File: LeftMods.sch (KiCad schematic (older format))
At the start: 9 parts

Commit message: Change and update leftmods
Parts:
- removed LM2: MX-1.5U, MX_Alps_Hybrid:MX-1.5U-NoLED, symbol MX-1U
- LM1: value MX-1.25U -> MX-1.5U; footprint MX_Alps_Hybrid:MX-1.25U-NoLED -> MX_Alps_Hybrid:MX-1.5U-NoLED
- LM2: renamed from LM3; value MX-1.25U -> MX-1U; footprint MX_Alps_Hybrid:MX-1.25U-NoLED -> MX_Alps_Hybrid:MX-1U-NoLED
- LM3: renamed from LM4; value MX-1U -> MX-1.25U; footprint MX_Alps_Hybrid:MX-1U-NoLED -> MX_Alps_Hybrid:MX-1.25U-NoLED
- LM4: renamed from LM5; value MX-1.25U -> MX-1.5U; footprint MX_Alps_Hybrid:MX-1.25U-NoLED -> MX_Alps_Hybrid:MX-1.5U-NoLED
- renumbered LM6 to LM5
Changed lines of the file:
@@
 P 2325 2225
 F 0 "LM1" H 2325 2350 60  0000 C CNN
-F 1 "MX-1.25U" H 2325 2275 20  0000 C CNN
-F 2 "MX_Alps_Hybrid:MX-1.25U-NoLED" H 2300 2200 60  0001 C CNN
+F 1 "MX-1.5U" H 2325 2275 20  0000 C CNN
+F 2 "MX_Alps_Hybrid:MX-1.5U-NoLED" H 2300 2200 60  0001 C CNN
 F 3 "" H 2300 2200 60  0001 C CNN
 	1    2325 2225
@@
 	0    -1   -1   0
 $EndComp
-Wire Wire Line
-	2150 2400 2300 2400
 $Comp
-L MX-1U LM3
+L MX-1U LM2
 U 1 1 5A68E96A
 P 2775 2225
-F 0 "LM3" H 2775 2350 60  0000 C CNN
-F 1 "MX-1.25U" H 2775 2275 20  0000 C CNN
-F 2 "MX_Alps_Hybrid:MX-1.25U-NoLED" H 2750 2200 60  0001 C CNN
+F 0 "LM2" H 2775 2350 60  0000 C CNN
+F 1 "MX-1U" H 2775 2275 20  0000 C CNN
+F 2 "MX_Alps_Hybrid:MX-1U-NoLED" H 2750 2200 60  0001 C CNN
 F 3 "" H 2750 2200 60  0001 C CNN
 	1    2775 2225
@@
 	2600 2400 2750 2400
 $Comp
-L MX-1U LM5
+L MX-1U LM4
 U 1 1 5A68E979
 P 3225 2225
-F 0 "LM5" H 3225 2350 60  0000 C CNN
-F 1 "MX-1.25U" H 3225 2275 20  0000 C CNN
-F 2 "MX_Alps_Hybrid:MX-1.25U-NoLED" H 3200 2200 60  0001 C CNN
+F 0 "LM4" H 3225 2350 60  0000 C CNN
+F 1 "MX-1.5U" H 3225 2275 20  0000 C CNN
+F 2 "MX_Alps_Hybrid:MX-1.5U-NoLED" H 3200 2200 60  0001 C CNN
 F 3 "" H 3200 2200 60  0001 C CNN
 	1    3225 2225
@@
 	3050 2400 3200 2400
 $Comp
-L MX-1U LM2
-U 1 1 5A68E988
-P 2325 2850
-F 0 "LM2" H 2325 2975 60  0000 C CNN
-F 1 "MX-1.5U" H 2325 2900 20  0000 C CNN
-F 2 "MX_Alps_Hybrid:MX-1.5U-NoLED" H 2300 2825 60  0001 C CNN
-F 3 "" H 2300 2825 60  0001 C CNN
-	1    2325 2850
-	1    0    0    -1
-$EndComp
-Wire Wire Line
-	2150 3025 2300 3025
-$Comp
-L MX-1U LM4
+L MX-1U LM3
 U 1 1 5A68E997
 P 2775 2850
-F 0 "LM4" H 2775 2975 60  0000 C CNN
-F 1 "MX-1U" H 2775 2900 20  0000 C CNN
-F 2 "MX_Alps_Hybrid:MX-1U-NoLED" H 2750 2825 60  0001 C CNN
+F 0 "LM3" H 2775 2975 60  0000 C CNN
+F 1 "MX-1.25U" H 2775 2900 20  0000 C CNN
+F 2 "MX_Alps_Hybrid:MX-1.25U-NoLED" H 2750 2825 60  0001 C CNN
 F 3 "" H 2750 2825 60  0001 C CNN
 	1    2775 2850
@@
 	2600 3025 2750 3025
 $Comp
-L MX-1U LM6
+L MX-1U LM5
 U 1 1 5A68E9A6
 P 3225 2850
-F 0 "LM6" H 3225 2975 60  0000 C CNN
+F 0 "LM5" H 3225 2975 60  0000 C CNN
 F 1 "MX-1.5U" H 3225 2900 20  0000 C CNN
 F 2 "MX_Alps_Hybrid:MX-1.5U-NoLED" H 3200 2825 60  0001 C CNN
@@
 	2600 2400 2600 3025
 Connection ~ 2675 2400
-Wire Wire Line
-	2150 2400 2150 3025
-Connection ~ 2225 2400
-Wire Wire Line
-	2500 1700 2500 2825
 Text GLabel 2500 1700 1    60   Input ~ 0
 COL0
@@
 Connection ~ 2225 2600
 Connection ~ 2675 2600
-Connection ~ 2500 2200
 Connection ~ 2950 2200
 Connection ~ 3400 2200
 Connection ~ 2800 2350
-Connection ~ 2350 2350
+Wire Wire Line
+	2500 1700 2500 2200
+Wire Wire Line
+	2225 2400 2300 2400
 $EndSCHEMATC

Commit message: Place LEDs and move out diodes
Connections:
- net COL2: now also LM5.2 (ROW); no longer LM5.1 (COL)
- net at D62.2 (A), LM4.2 (ROW): now also LM5.1 (COL); no longer LM5.2 (ROW)
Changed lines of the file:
@@
 $EndComp
 Wire Wire Line
-	3050 2400 3200 2400
+	3125 2400 3525 2400
 $Comp
 L MX-1U LM3
@@
 	1    0    0    -1
 $EndComp
-Wire Wire Line
-	3050 3025 3200 3025
-Wire Wire Line
-	3050 2400 3050 3025
 Connection ~ 3125 2400
 Wire Wire Line
@@
 COL1
 Wire Wire Line
-	3400 1700 3400 2825
+	3400 1700 3400 2675
 Text GLabel 3400 1700 1    60   Input ~ 0
 COL2
@@
 Wire Wire Line
 	2225 2400 2300 2400
+Wire Wire Line
+	3400 2675 3200 2675
+Wire Wire Line
+	3200 2675 3200 3025
+Wire Wire Line
+	3525 2400 3525 2825
+Wire Wire Line
+	3525 2825 3400 2825
+Connection ~ 3200 2400
 $EndSCHEMATC

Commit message: Revert LED structure
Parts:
- LM1, LM4, LM5: footprint MX_Alps_Hybrid:MX-1.5U-NoLED -> MX_Alps_Hybrid:MX-1.5U
- LM2: footprint MX_Alps_Hybrid:MX-1U-NoLED -> MX_Alps_Hybrid:MX-1U
- LM3: footprint MX_Alps_Hybrid:MX-1.25U-NoLED -> MX_Alps_Hybrid:MX-1.25U
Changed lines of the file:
@@
 F 0 "LM1" H 2325 2350 60  0000 C CNN
 F 1 "MX-1.5U" H 2325 2275 20  0000 C CNN
-F 2 "MX_Alps_Hybrid:MX-1.5U-NoLED" H 2300 2200 60  0001 C CNN
+F 2 "MX_Alps_Hybrid:MX-1.5U" H 2300 2200 60  0001 C CNN
 F 3 "" H 2300 2200 60  0001 C CNN
 	1    2325 2225
@@
 F 0 "LM2" H 2775 2350 60  0000 C CNN
 F 1 "MX-1U" H 2775 2275 20  0000 C CNN
-F 2 "MX_Alps_Hybrid:MX-1U-NoLED" H 2750 2200 60  0001 C CNN
+F 2 "MX_Alps_Hybrid:MX-1U" H 2750 2200 60  0001 C CNN
 F 3 "" H 2750 2200 60  0001 C CNN
 	1    2775 2225
@@
 F 0 "LM4" H 3225 2350 60  0000 C CNN
 F 1 "MX-1.5U" H 3225 2275 20  0000 C CNN
-F 2 "MX_Alps_Hybrid:MX-1.5U-NoLED" H 3200 2200 60  0001 C CNN
+F 2 "MX_Alps_Hybrid:MX-1.5U" H 3200 2200 60  0001 C CNN
 F 3 "" H 3200 2200 60  0001 C CNN
 	1    3225 2225
@@
 F 0 "LM3" H 2775 2975 60  0000 C CNN
 F 1 "MX-1.25U" H 2775 2900 20  0000 C CNN
-F 2 "MX_Alps_Hybrid:MX-1.25U-NoLED" H 2750 2825 60  0001 C CNN
+F 2 "MX_Alps_Hybrid:MX-1.25U" H 2750 2825 60  0001 C CNN
 F 3 "" H 2750 2825 60  0001 C CNN
 	1    2775 2850
@@
 F 0 "LM5" H 3225 2975 60  0000 C CNN
 F 1 "MX-1.5U" H 3225 2900 20  0000 C CNN
-F 2 "MX_Alps_Hybrid:MX-1.5U-NoLED" H 3200 2825 60  0001 C CNN
+F 2 "MX_Alps_Hybrid:MX-1.5U" H 3200 2825 60  0001 C CNN
 F 3 "" H 3200 2825 60  0001 C CNN
 	1    3225 2850

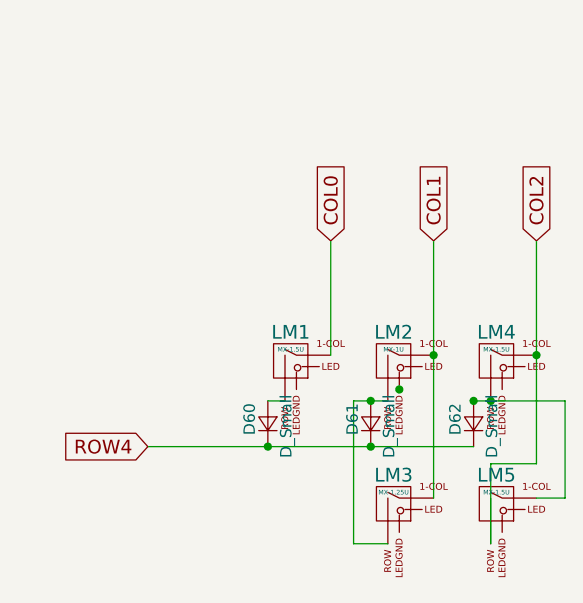
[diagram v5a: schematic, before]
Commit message: Wire LED rows
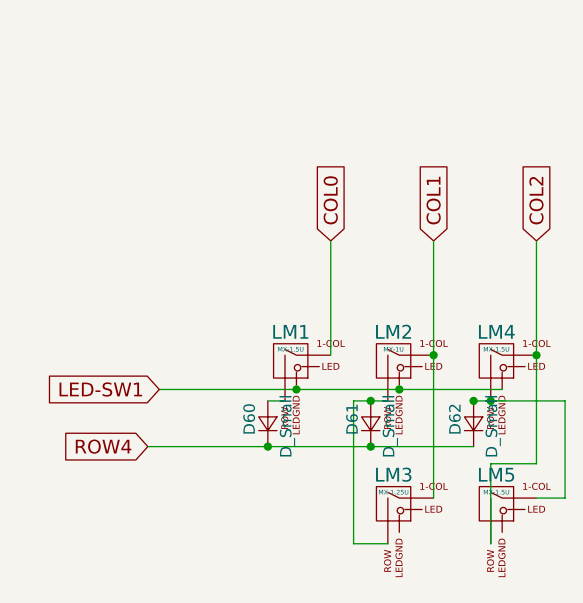
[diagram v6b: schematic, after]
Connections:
- net LED-SW1: now reaches LM1.4 (LEDGND)
- net LED-SW1: now also LM2.4 (LEDGND), LM4.4 (LEDGND)
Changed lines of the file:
@@
 Wire Wire Line
 	3525 2400 3525 2825
+Wire Wire Line
+	1750 2350 3250 2350
+Connection ~ 2350 2350
+Text GLabel 1750 2350 0    60   Input ~ 0
+LED-SW1
 $EndSCHEMATC

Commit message: Begin routing
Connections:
- net LED-CS1: now reaches LM1.3 (LED)
- net LED-CS2: now reaches LM2.3 (LED)
- net LED-CS3: now reaches LM4.3 (LED)
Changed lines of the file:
@@
 Text GLabel 1750 2350 0    60   Input ~ 0
 LED-SW1
+Wire Wire Line
+	2450 2250 2450 1325
+Text GLabel 2450 1325 1    60   Input ~ 0
+LED-CS1
+Wire Wire Line
+	2900 1325 2900 2250
+Text GLabel 2900 1325 1    60   Input ~ 0
+LED-CS2
+Wire Wire Line
+	3350 2250 3350 1325
+Text GLabel 3350 1325 1    60   Input ~ 0
+LED-CS3
 $EndSCHEMATC

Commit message: Temporary save before rollback
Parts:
- LM3: footprint MX_Alps_Hybrid:MX-1.25U -> MX_Alps_Hybrid:MX-1.25U-FLIPPED
- LM5: footprint MX_Alps_Hybrid:MX-1.5U -> MX_Alps_Hybrid:MX-1.5U-FLIPPED
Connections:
- net LED-CS2: now also LM3.3 (LED)
- net LED-CS3: now also LM5.3 (LED)
- net LED-SW1: now also LM3.4 (LEDGND), LM5.4 (LEDGND)
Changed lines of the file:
@@
 F 0 "LM3" H 2775 2975 60  0000 C CNN
 F 1 "MX-1.25U" H 2775 2900 20  0000 C CNN
-F 2 "MX_Alps_Hybrid:MX-1.25U" H 2750 2825 60  0001 C CNN
+F 2 "MX_Alps_Hybrid:MX-1.25U-FLIPPED" H 2750 2825 60  0001 C CNN
 F 3 "" H 2750 2825 60  0001 C CNN
 	1    2775 2850
@@
 F 0 "LM5" H 3225 2975 60  0000 C CNN
 F 1 "MX-1.5U" H 3225 2900 20  0000 C CNN
-F 2 "MX_Alps_Hybrid:MX-1.5U" H 3200 2825 60  0001 C CNN
+F 2 "MX_Alps_Hybrid:MX-1.5U-FLIPPED" H 3200 2825 60  0001 C CNN
 F 3 "" H 3200 2825 60  0001 C CNN
 	1    3225 2850
@@
 LED-CS1
 Wire Wire Line
-	2900 1325 2900 2250
+	2900 1325 2900 2875
 Text GLabel 2900 1325 1    60   Input ~ 0
 LED-CS2
 Wire Wire Line
-	3350 2250 3350 1325
+	3350 1325 3350 2875
 Text GLabel 3350 1325 1    60   Input ~ 0
 LED-CS3
+Connection ~ 2900 2250
+Wire Wire Line
+	2800 2350 2800 2975
+Connection ~ 3350 2250
+Wire Wire Line
+	3250 2350 3250 2975
 $EndSCHEMATC
